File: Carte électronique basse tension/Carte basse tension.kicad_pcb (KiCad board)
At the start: 2 copper layers, 60 x 62.5 mm, 22 parts

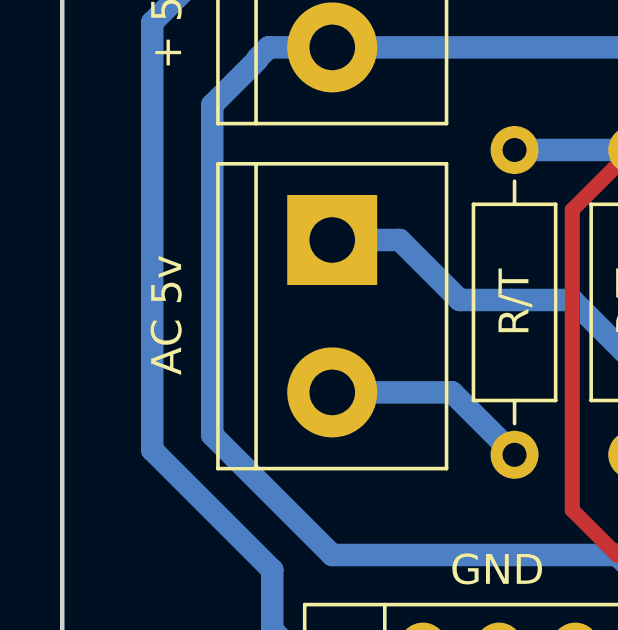
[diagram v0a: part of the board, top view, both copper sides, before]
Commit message: ajout carte interface microcontroleur - régulateur
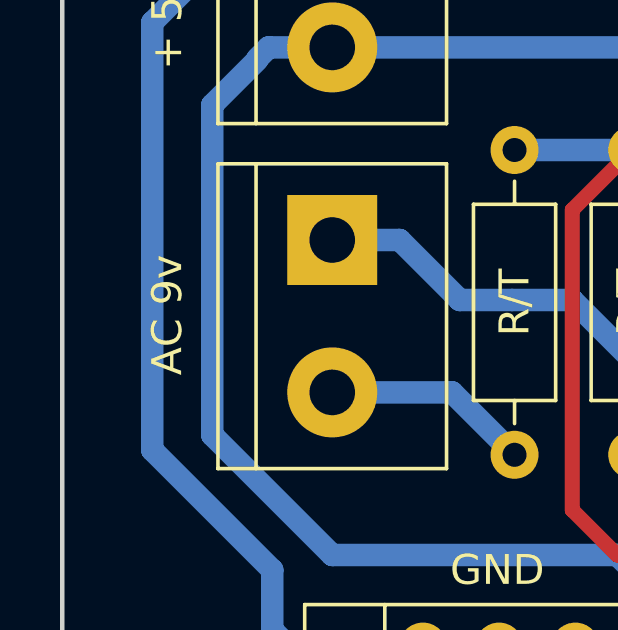
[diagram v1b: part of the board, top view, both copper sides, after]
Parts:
- AC 9v: renamed from AC 5v
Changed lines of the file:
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@@
     (descr "simple 2-pin terminal block, pitch 5.08mm, revamped version of bornier2")
     (tags "terminal block bornier2")
-    (fp_text reference "AC 5v" (at 2.5 5.5 270) (layer F.SilkS)
+    (fp_text reference "AC 9v" (at 2.5 5.5 270) (layer F.SilkS)
       (effects (font (size 1 1) (thickness 0.15)))
     )
